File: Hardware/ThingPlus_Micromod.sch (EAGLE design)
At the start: 70 parts, among them J4 QWIIC_RIGHT_ANGLE, J5 MICRO-SD-SDIOPUSH-PUSH, J6 JTAG, J7 MICROMOD-2222-C, U2 MCP73831, U3 MAX17048, U4 3.3V, U6 AP7361C-33

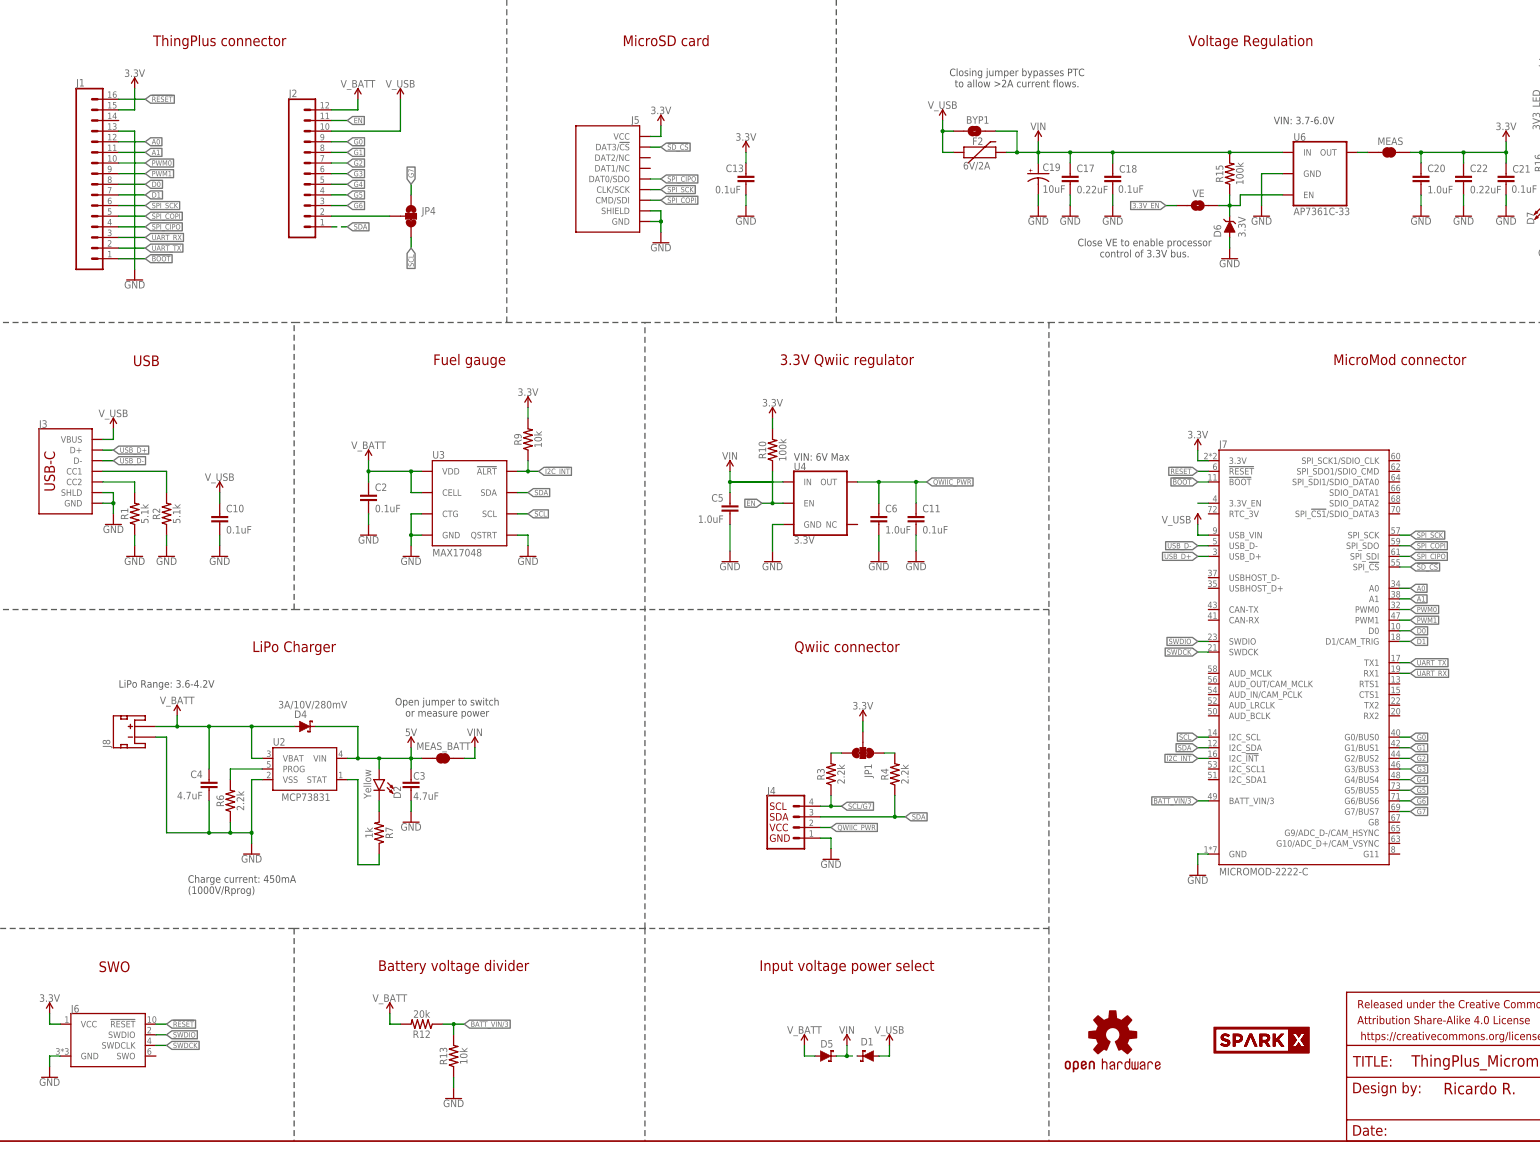
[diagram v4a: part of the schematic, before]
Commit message: Rename SCL/G7 net to SCL.
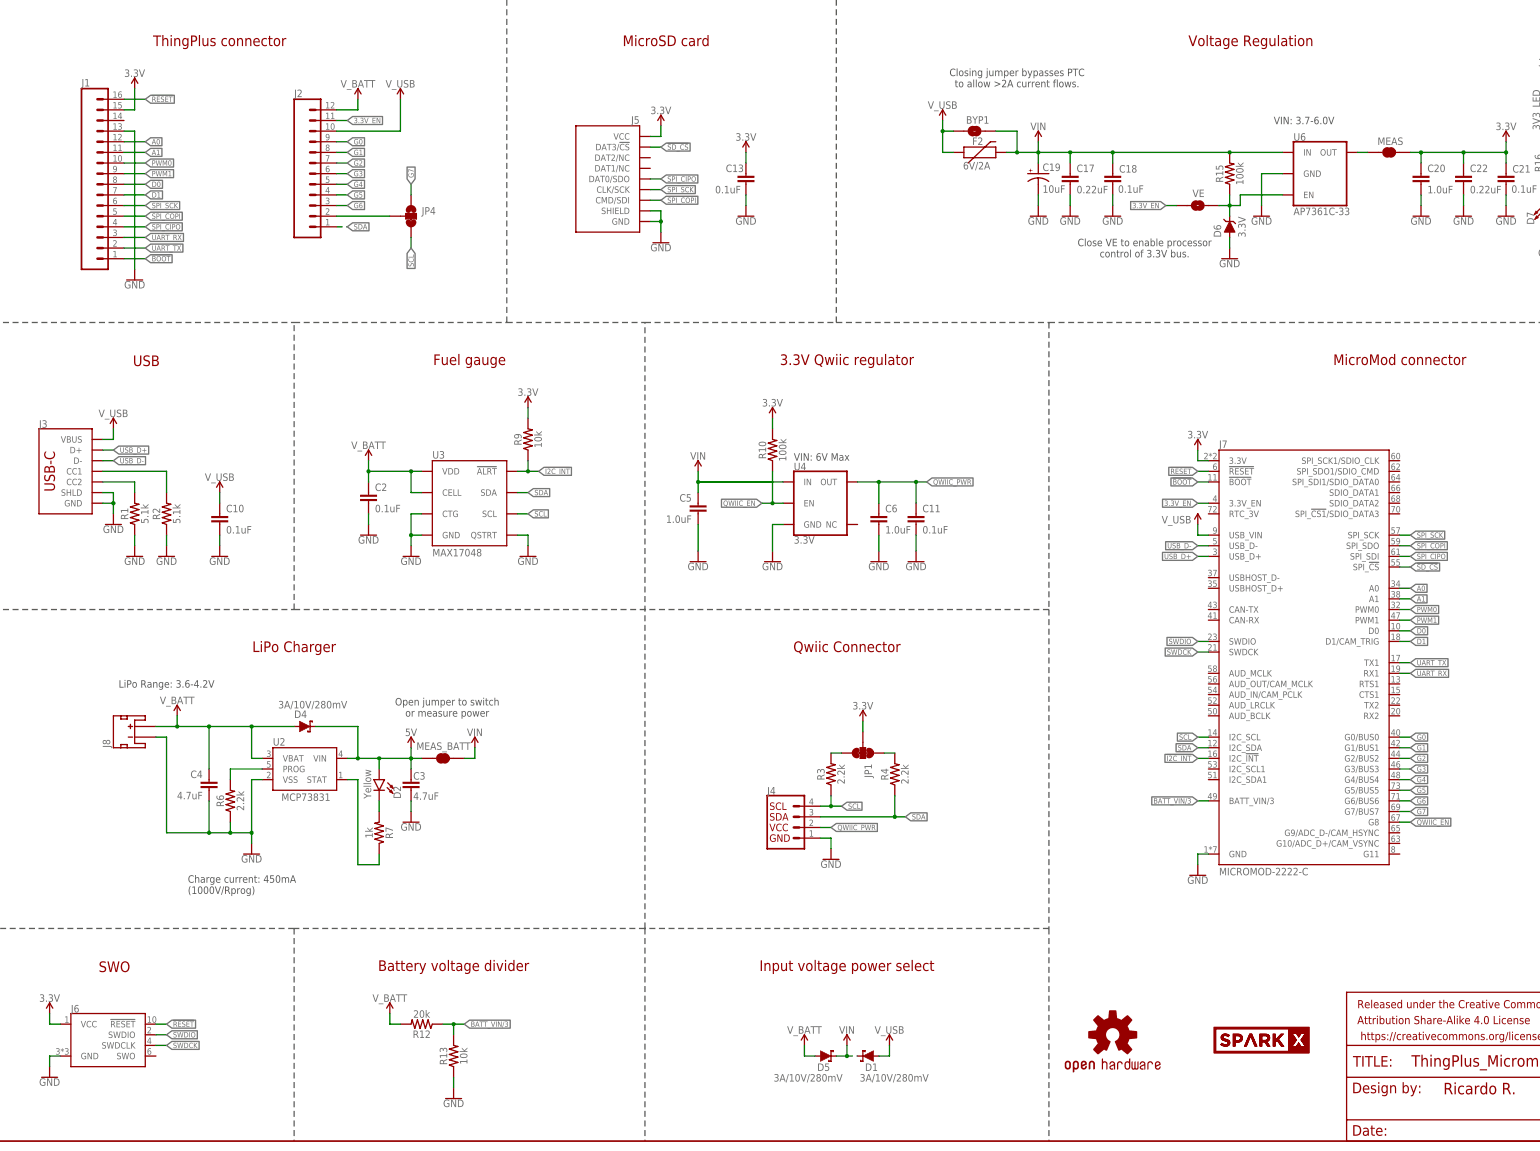
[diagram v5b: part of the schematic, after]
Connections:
- removed net EN: J2.11, R10.1, U4.EN
- removed net SCL/G7: J4.4, R3.1
- new net QWIIC_EN: J7.G8, R10.1, U4.EN
- net 3.3V_EN: now also J2.11
- net SCL: now also J4.4, R3.1
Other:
- note added: "Qwiic Connector"
- note removed: "Qwiic connector"
- moved on the sheet: C5, J1, J2

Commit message: Moved components to remove clearance errors; optimized GND and VCC polygons; fixed schematic off-grid components and fixed CamelCasing. TODO: add labels.
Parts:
- added FD2, FD3: FIDUCIALUFIDUCIAL, SparkFun-Aesthetics:FIDUCIALUFIDUCIAL
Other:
- note added: "3.3V Qwiic Regulator"
- note added: "Battery Voltage Divider"
- note added: "Fuel Gauge"
- note added: "Input Voltage Power Select"
- note added: "MicroMod Connector"
- note added: "MicroSD Card"
- note added: "ThingPlus Connector"
- note removed: "3.3V Qwiic regulator"
- note removed: "Battery voltage divider"
- note removed: "Fuel gauge"
- note removed: "Input voltage power select"
- note removed: "MicroMod connector"
- note removed: "MicroSD card"
- note removed: "ThingPlus connector"
- moved on the sheet: 3V3_LED, C13, D7, D8, J4, J5, JP1, R16, R17, R3, R4, VIN_LED

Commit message: Added buzzard labels to ThingPlus MicroMod
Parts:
- added LOGO2, LOGO3: QWIIC_LOGO_4MM, SparkFun-Aesthetics:QWIIC_LOGO_4MM
- U$2: value SPARKX-LOGO2 -> SPARKX-LOGO4; device SparkX:SPARKX-LOGO2 -> SparkX:SPARKX-LOGO4
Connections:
- net !RESET! renamed !RST!
- net 3.3V_EN renamed EN
- net N$5 renamed SCL/G7

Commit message: Updated layout per Nathan's recommendations
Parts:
- removed C17, C22: 0.22uF, SparkFun-Capacitors:0.22UF-0603-25V-10%
- removed C18, C21: 0.1uF, SparkFun-Capacitors:0.1UF-0603-25V-(+80/-20%)
- removed C19: 10uF, SparkFun-Capacitors:10UF-POLAR-EIA3216-16V-10%(TANT)
- removed C20: 1.0uF, SparkFun-Capacitors:1.0UF-0603-16V-10%
- removed D7: RED, SparkFun-LED:LED-RED0603
- removed D8: Yellow, SparkFun-LED:LED-YELLOW0603
- removed F2: 6V/2A, SparkFun-Fuses:PPTC_6V2A
- removed MEAS, MEAS_BATT: JUMPER-COMBO_2_NC_TRACE, SparkFun-Jumpers:JUMPER-COMBO_2_NC_TRACE
- removed R15: 100k, SparkFun-Resistors:100KOHM-0603-1/10W-1%
- removed R16: 1k, SparkFun-Resistors:1KOHM-0603-1/10W-1%
- removed R17: 4.7k, SparkFun-Resistors:4.7KOHM-0603-1/10W-1%
- removed U6: AP7361C-33, SparkFun-IC-Power:AP7361C-33FGEUDFN-8
- added C1, C14: 0.1uF, SparkFun-Capacitors:0.1UF-0603-25V-(+80/-20%)
- added C12: 1.0uF, SparkFun-Capacitors:1.0UF-0603-16V-10%
- added C15: 4.7uF, SparkFun-Capacitors:4.7UF-0603-6.3V-(10%)
- added C16: 4.7uF, SparkFun-Capacitors:4.7UF-0603-35V-(20%)
- added C9: 0.22uF, SparkFun-Capacitors:0.22UF-0603-25V-10%
- added CURR_MEAS: JUMPER-COMBO_2_NC_TRACE, SparkFun-Jumpers:JUMPER-COMBO_2_NC_TRACE
- added D3: 3A/10V/280mV, SparkFun-DiscreteSemi:DIODE-SCHOTTKY-BAT60A
- added F1: 6V/2A, SparkFun-Fuses:PPTC_6V2A
- added R11: 10k, SparkFun-Resistors:10KOHM-0603-1/10W-1%
- added R5: 100k, SparkFun-Resistors:100KOHM-0603-1/10W-1%
- added R8: 2.2k, SparkFun-Resistors:2.2KOHM-0603-1/10W-1%
- added U64: AP7361C-33, SparkFun-IC-Power:AP7361C-33FGEUDFN-8
- C13, C2, C8: value 0.1uF -> 1.0uF; device SparkFun-Capacitors:0.1UF-0603-25V-(+80/-20%) -> SparkFun-Capacitors:1.0UF-0603-16V-10%
- C3: value 4.7uF -> 0.1uF; device SparkFun-Capacitors:4.7UF-0603-35V-(20%) -> SparkFun-Capacitors:0.1UF-0603-25V-(+80/-20%)
- C4: value 4.7uF -> 0.1uF; device SparkFun-Capacitors:4.7UF-0603-6.3V-(10%) -> SparkFun-Capacitors:0.1UF-0603-25V-(+80/-20%)
- C5: value 1.0uF -> 10uF; device SparkFun-Capacitors:1.0UF-0603-16V-10% -> SparkFun-Capacitors:10UF-0805-25V-10%
- C6: value 1.0uF -> 0.22uF; device SparkFun-Capacitors:1.0UF-0603-16V-10% -> SparkFun-Capacitors:0.22UF-0603-25V-10%
- C7: value 1.0uF -> 0.1uF; device SparkFun-Capacitors:1.0UF-0603-16V-10% -> SparkFun-Capacitors:0.1UF-0603-25V-(+80/-20%)
- D1: value 3A/10V/280mV -> 3.3V; device SparkFun-DiscreteSemi:DIODE-SCHOTTKY-BAT60A -> SparkFun-DiscreteSemi:DIODE-ZENER-MM3Z3V3T1G
- D5: value 3A/10V/280mV -> RED; device SparkFun-DiscreteSemi:DIODE-SCHOTTKY-BAT60A -> SparkFun-LED:LED-RED0603
- D6: value 3.3V -> Yellow; device SparkFun-DiscreteSemi:DIODE-ZENER-MM3Z3V3T1G -> SparkFun-LED:LED-YELLOW0603
- J1: value (none) -> MICROMOD-2222-C; device SparkFun-Connectors:CONN_161X16_SM_SQ_NOSILK -> SparkFun-MicroMod:MICROMOD-2222-C
- J2: device SparkFun-Connectors:CONN_12SM_SQ_NO_SILK -> SparkFun-Connectors:CONN_161X16_SM_SQ_NOSILK
- J3: device SparkFun-Connectors:USB_C_4-LAYER_PADS -> SparkFun-Connectors:CONN_12SM_SQ_NO_SILK
- J4: value QWIIC_RIGHT_ANGLE -> MICRO-SD-SDIOPUSH-PUSH; device SparkFun-Connectors:QWIIC_CONNECTORJS-1MM -> SparkFun-Connectors:MICRO-SD-SDIOPUSH-PUSH
- J5: value MICRO-SD-SDIOPUSH-PUSH -> (none); device SparkFun-Connectors:MICRO-SD-SDIOPUSH-PUSH -> SparkFun-Connectors:USB_C_4-LAYER_PADS
- J6: value JTAG -> (none); device SparkFun-Connectors:CORTEX_JTAG_DEBUG_MINIMUM_PTH -> SparkFun-Connectors:JST_2MM_MALE
- J7: value MICROMOD-2222-C -> QWIIC_RIGHT_ANGLE; device SparkFun-MicroMod:MICROMOD-2222-C -> SparkFun-Connectors:QWIIC_CONNECTORJS-1MM
- J8: value (none) -> JTAG; device SparkFun-Connectors:JST_2MM_MALE -> SparkFun-Connectors:CORTEX_JTAG_DEBUG_MINIMUM_PTH
- LOGO1: value OSHW-LOGOS -> OSHW-LOGOMINI; device SparkFun-Aesthetics:OSHW-LOGOS -> SparkFun-Aesthetics:OSHW-LOGOMINI
- R10: value 100k -> 20k; device SparkFun-Resistors:100KOHM-0603-1/10W-1% -> SparkFun-Resistors:20KOHM-0603-1/10W-1%
- R12: value 20k -> 1k; device SparkFun-Resistors:20KOHM-0603-1/10W-1% -> SparkFun-Resistors:1KOHM-0603-1/10W-1%
- R13: value 10k -> 4.7k; device SparkFun-Resistors:10KOHM-0603-1/10W-1% -> SparkFun-Resistors:4.7KOHM-0603-1/10W-1%
- R3: value 2.2k -> 100k; device SparkFun-Resistors:2.2KOHM-0603-1/10W-1% -> SparkFun-Resistors:100KOHM-0603-1/10W-1%
- R4: value 2.2k -> 10k; device SparkFun-Resistors:2.2KOHM-0603-1/10W-1% -> SparkFun-Resistors:10KOHM-0603-1/10W-1%
- R9: value 10k -> 2.2k; device SparkFun-Resistors:10KOHM-0603-1/10W-1% -> SparkFun-Resistors:2.2KOHM-0603-1/10W-1%
- U$1: value SPARKX-LOGO2 -> SPARKX-LOGO5; device SparkX:SPARKX-LOGO2 -> SparkX:SPARKX-LOGO5
- U$2: value SPARKX-LOGO4 -> SPARKX-LOGO5; device SparkX:SPARKX-LOGO4 -> SparkX:SPARKX-LOGO5
- renumbered JP4 to SCL/G7, U2 to U27, U3 to U34, U4 to U44
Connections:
- removed net 5V: C3.1, D2.A, D4.C, MEAS_BATT.1, U27.VIN
- removed net N$1: MEAS.1, U6.OUT
- new net N$2: JP1.3, R8.2
- new net N$5: CURR_MEAS.1, D3.C, D4.C
- net !BOOT!: now also J1.!BOOT!, J2.1; no longer J1.1, J7.!BOOT!
- net !I2C_INT!: now also J1.I2C_!INT!, R4.1; no longer J7.I2C_!INT!, R9.1
- net !RST!: now also J1.!RESET!, J2.16, J8.!RESET; no longer J1.16, J6.!RESET, J7.!RESET!
- net !SD_CS!: now also J1.SPI_!CS!, J4.DAT3/!CS!; no longer J5.DAT3/!CS!, J7.SPI_!CS!
- net 3.3V: now also C1.2, C10.1, C2.2, C4.1, C8.1, C9.1, J1.3.3V, J2.15, J4.VCC, J8.VCC, R4.2, R5.2, U64.OUT; no longer C13.1, C20.1, C21.1, C22.1, C7.2, C8.2, J1.15, J5.VCC, J6.VCC, J7.3.3V, MEAS.2, R10.2, R9.2
- net 3.3V_EN_VE: now also D1.C, R3.1, U64.EN; no longer D6.C, R15.1, U6.EN
- net A0: now also J1.A0, J2.12; no longer J1.12, J7.A0
- net A1: now also J1.A1, J2.11; no longer J1.11, J7.A1
- net BATT_VIN/3: now also J1.BATT_VIN/3, R10.1, R11.2; no longer J7.BATT_VIN/3, R12.1, R13.2
- net D0: now also J1.D0, J2.8; no longer J1.8, J7.D0
- net D1: now also J1.D1/CAM_TRIG, J2.7; no longer J1.7, J7.D1/CAM_TRIG
- net EN: now also J1.3.3V_EN, J3.11; no longer J2.11, J7.3.3V_EN
- net G0: now also J1.G0/BUS0, J3.9; no longer J2.9, J7.G0/BUS0
- net G1: now also J1.G1/BUS1, J3.8; no longer J2.8, J7.G1/BUS1
- net G2: now also J1.G2/BUS2, J3.7; no longer J2.7, J7.G2/BUS2
- net G3: now also J1.G3/BUS3, J3.6; no longer J2.6, J7.G3/BUS3
- net G4: now also J1.G4/BUS4, J3.5; no longer J2.5, J7.G4/BUS4
- net G5: now also J1.G5/BUS5, J3.4; no longer J2.4, J7.G5/BUS5
- net G6: now also J1.G6/BUS6, J3.3; no longer J2.3, J7.G6/BUS6
- net G7: now also J1.G7/BUS7; no longer J7.G7/BUS7
- net GND: now also C1.1, C12.2, C14.2, C15.2, C16.2, C2.1, C7.2, C8.2, C9.2, D1.A, D5.C, D6.C, J1.GND, J2.13, J4.GND, J4.SHIELD, J5.SHLD, J6.-, J7.1, J8.GND, R11.1, U64.GND; no longer C17.2, C18.2, C19.-, C2.2, C20.2, C21.2, C22.2, C7.1, C8.1, D6.A, D7.C, D8.C, J1.13, J3.GND, J3.SHLD, J4.1, J5.SHIELD, J6.GND, J7.GND, J8.-, R13.1, U6.GND
- net N$10: now also R13.2; no longer R17.2
- net N$11: now also D6.A, R13.1; no longer D8.A, R17.1
- net N$12: now also J5.CC1; no longer J3.CC1
- net N$13: now also J5.CC2; no longer J3.CC2
- net N$3: now also JP1.1, R9.2; no longer JP1.3, R3.2
- net N$4: now also BYP1.2, D3.A, F1.2; no longer JP1.1, R4.2
- net N$6: now also R12.2; no longer R16.2
- net N$9: now also D5.A, R12.1; no longer D7.A, R16.1
- net PWM0: now also J1.PWM0, J2.10; no longer J1.10, J7.PWM0
- net PWM1: now also J1.PWM1, J2.9; no longer J1.9, J7.PWM1
- net QWIIC_EN: now also J1.G8, R5.1; no longer J7.G8, R10.1
- net QWIIC_PWR: now also C13.1, C14.1, J7.2; no longer C11.1, C6.1, J4.2
- net SCL: now also J1.I2C_SCL, J7.4, R8.1; no longer J4.4, J7.I2C_SCL, R3.1
- net SCL/G7: now also J3.2; no longer J2.2
- net SDA: now also J1.I2C_SDA, J3.1, J7.3, R9.1; no longer J2.1, J4.3, J7.I2C_SDA, R4.1
- net SPI_CIPO: now also J1.SPI_SDI, J2.4, J4.DAT0/SDO; no longer J1.4, J5.DAT0/SDO, J7.SPI_SDI
- net SPI_COPI: now also J1.SPI_SDO, J2.5, J4.CMD/SDI; no longer J1.5, J5.CMD/SDI, J7.SPI_SDO
- net SPI_SCK: now also J1.SPI_SCK, J2.6, J4.CLK/SCK; no longer J1.6, J5.CLK/SCK, J7.SPI_SCK
- net SWDCK: now also J1.SWDCK, J8.SWDCLK; no longer J6.SWDCLK, J7.SWDCK
- net SWDIO: now also J1.SWDIO, J8.SWDIO; no longer J6.SWDIO, J7.SWDIO
- net UART_RX: now also J1.RX1, J2.3; no longer J1.3, J7.RX1
- net UART_TX: now also J1.TX1, J2.2; no longer J1.2, J7.TX1
- net USB_D+: now also J1.USB_D+, J5.D+; no longer J3.D+, J7.USB_D+
- net USB_D-: now also J1.USB_D-, J5.D-; no longer J3.D-, J7.USB_D-
- net VIN: now also C12.1, C16.1, C6.1, C7.1, CURR_MEAS.2, D2.A, R3.2, U27.VIN, U64.IN; no longer BYP1.2, C17.1, C18.1, C19.+, D1.C, D5.C, F2.2, MEAS_BATT.2, R15.2, U6.IN
- net V_BATT: now also C11.1, C15.1, J3.12, J6.+, R10.2; no longer C2.1, C4.1, D5.A, J2.12, J8.+, R12.2
- net V_USB: now also C3.1, F1.1, J1.USB_VIN, J3.10, J5.VBUS; no longer C10.1, D1.A, F2.1, J2.10, J3.VBUS, J7.USB_VIN
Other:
- note added: "Open jumper to measure charge current"
- note added: "Power LEDs"
- note removed: "Open jumper to switch or measure power"
- moved on the sheet: 3V3_LED, BYP1, C10, C11, C13, C2, C3, C4, C5, C6, C7, C8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
